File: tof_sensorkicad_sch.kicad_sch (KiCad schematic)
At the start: 1 part

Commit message: working on board
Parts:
- U2: footprint (none) -> 00_parts_lib:SATEL-VL53L8A
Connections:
- net +1.8VDC: now also U2.11 (IOVDD), U2.3 (CORE_1V8); no longer U2. (SDA)
- net +3.3VDC: now also U2.12 (AVDD); no longer U2. (SDA)
- net GND: now also U2.1 (DUT_GND), U2.7 (I2C_N); no longer U2. (SDA)
- net PWM_1: now also U2.4 (LPn); no longer U2. (SDA)
- net SCL: now also U2.8 (SCL); no longer U2. (SDA)
- net SDA: now also U2.6 (SDA); no longer U2. (SDA)
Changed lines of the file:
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@@
 		(dnp no)
 		(fields_autoplaced yes)
-		(property "Reference" "#PWR012"
+		(property "Reference" "#PWR014"
 			(at 165.1 113.03 0)
 			(effects
@@
 			(project ""
 				(path "/f7edb1cc-a42a-4cc0-9a6f-d9bd2b944353/74857e1b-d607-48d9-8b82-96dfc41384b6"
-					(reference "#PWR012")
+					(reference "#PWR014")
 					(unit 1)
 				)
@@
 			)
 		)
-		(property "Footprint" ""
+		(property "Footprint" "00_parts_lib:SATEL-VL53L8A"
 			(at 176.53 72.39 0)
 			(effects
@@
 			)
 		)
-		(pin ""
+		(pin "2"
 		)
-		(pin ""
+		(pin "3"
 		)
-		(pin ""
+		(pin "10"
 		)
-		(pin ""
+		(pin "8"
 		)
-		(pin ""
+		(pin "7"
 		)
-		(pin ""
+		(pin "11"
 		)
-		(pin ""
+		(pin "5"
 		)
-		(pin ""
+		(pin "1"
 		)
-		(pin ""
+		(pin "6"
 		)
-		(pin ""
+		(pin "9"
 		)
-		(pin ""
+		(pin "4"
 		)
-		(pin ""
+		(pin "12"
 		)
 		(instances

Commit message: made board
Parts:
- added TP10, TP11, TP12, TP13, TP14, TP9: TestPoint, TestPoint:TestPoint_Pad_D2.0mm, symbol Connector:TestPoint
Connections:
- net GND: now also TP12.1, TP13.1, TP14.1
- net PWM_1: now also TP11.1
- net SCL: now also TP9.1
- net SDA: now also TP10.1
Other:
- note added: "TEST POINTS"
- note added: "TOF CIRCUIT"
- moved on the sheet: U2

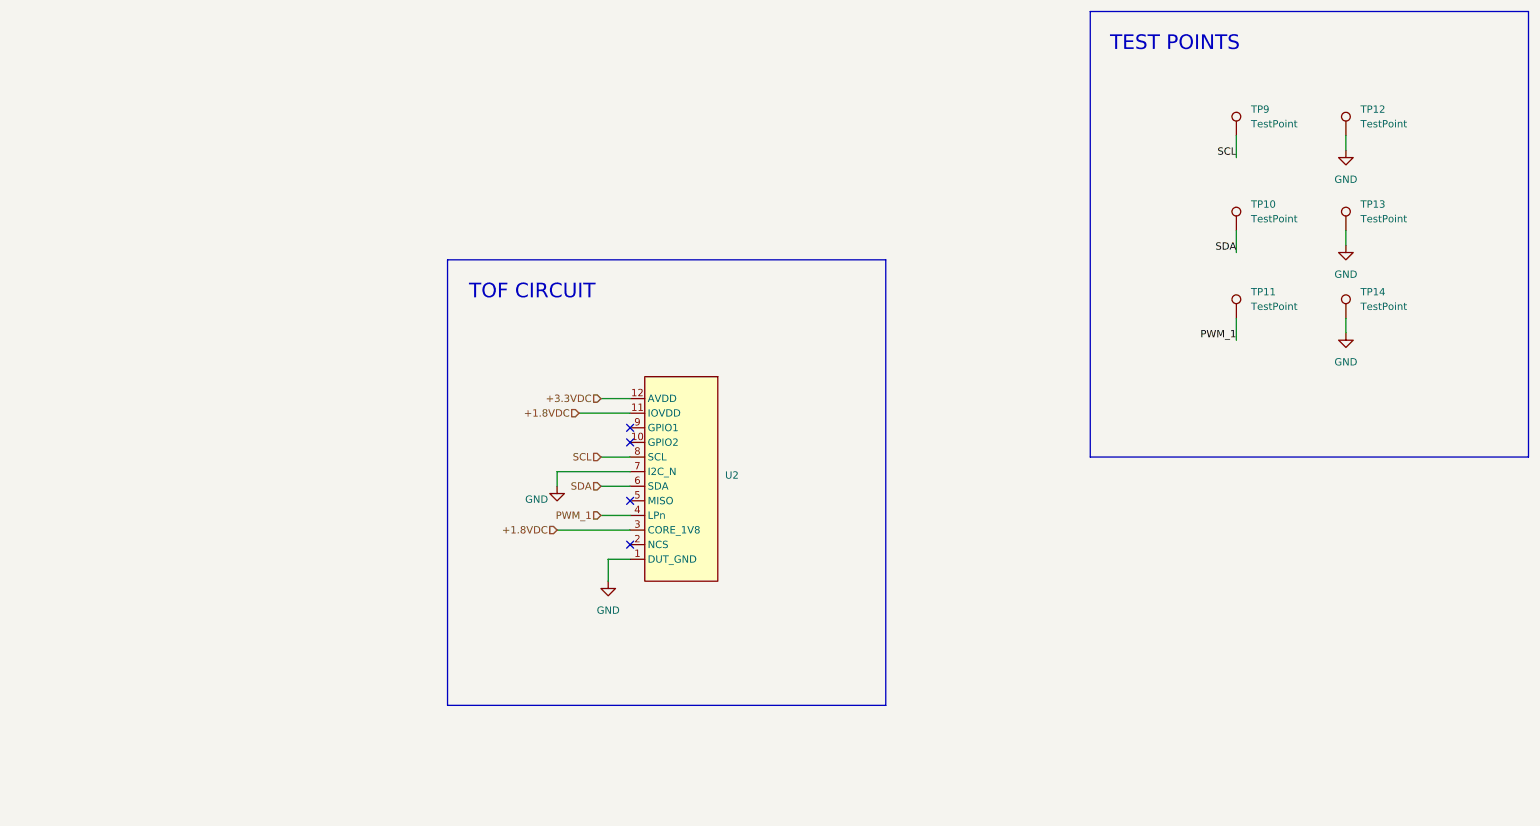
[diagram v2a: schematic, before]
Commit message: working on revisions
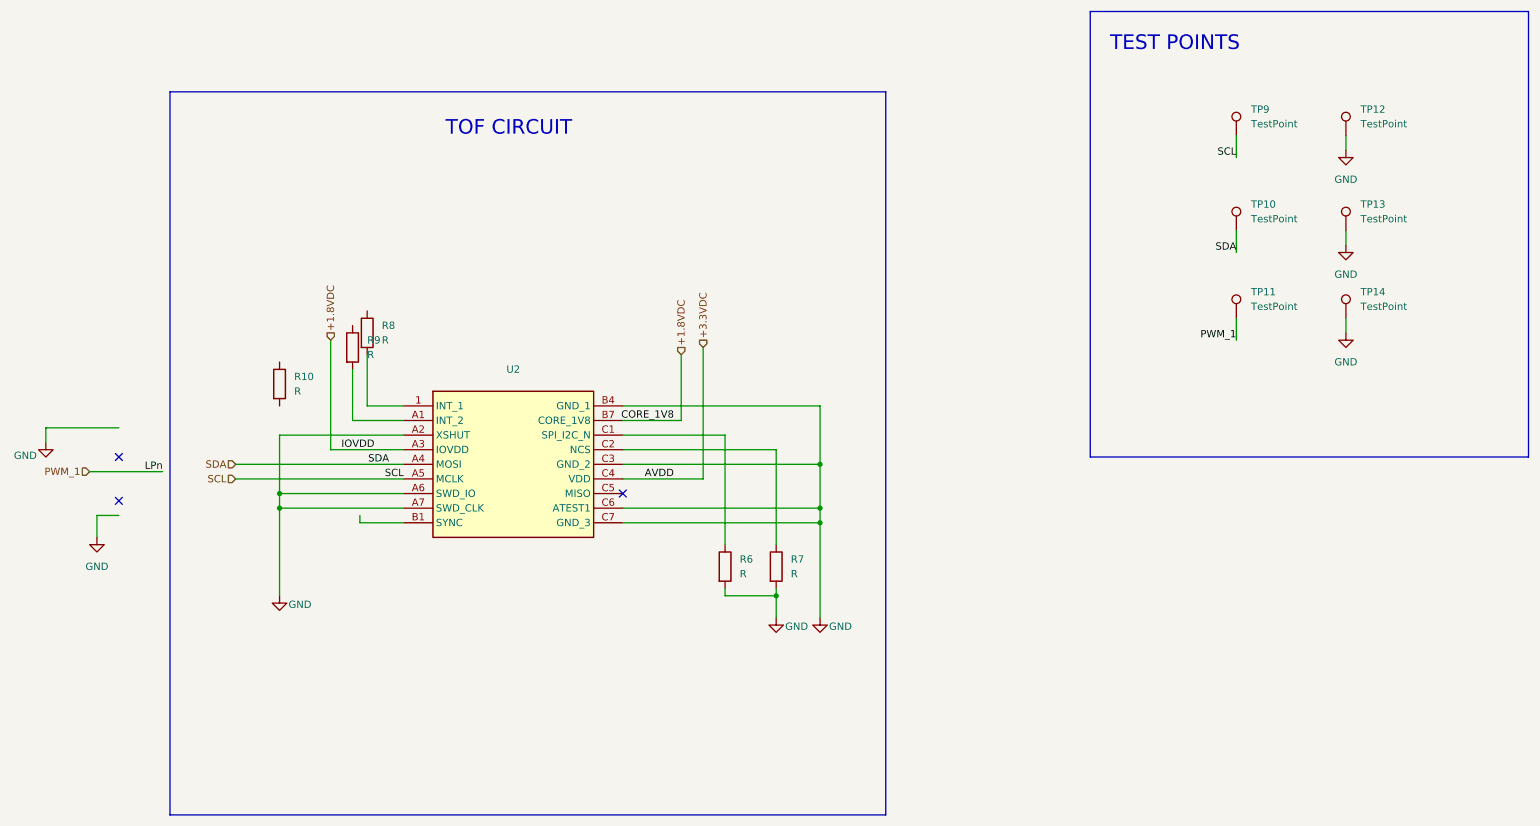
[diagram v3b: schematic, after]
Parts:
- added R10, R6, R7, R8, R9: R, Resistor_SMD:R_0805_2012Metric_Pad1.20x1.40mm_HandSolder, symbol Device:R
- U2: footprint 00_parts_lib:SATEL-VL53L8A -> VL53L8CXV0GC1; symbol 00_project_parts:SATEL-VL53L8A -> 00_project_parts:VL53L8CXV0GC_1; Height (none) -> 1.8; Manufacturer_Name (none) -> STMicroelectronics; Manufacturer_Part_Number (none) -> VL53L8CXV0GC/1; Mouser Part Number (none) -> 511-VL53L8CXV0GC/1; Mouser Price/Stock (none) -> https://www.mouser.co.uk/ProductDetail/STMicroelectronics/V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
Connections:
- net +1.8VDC: now also U2.A3 (IOVDD), U2.B7 (CORE_1V8); no longer U2.11 (IOVDD), U2.3 (CORE_1V8)
- net +3.3VDC: now also U2.C4 (VDD); no longer U2.12 (AVDD)
- net GND: now also U2.A2 (XSHUT), U2.A6 (SWD_IO), U2.A7 (SWD_CLK), U2.B4 (GND_1), U2.C3 (GND_2), U2.C6 (ATEST1), U2.C7 (GND_3), R6.2, R7.2; no longer U2.1 (DUT_GND), U2.7 (I2C_N)
- net PWM_1: no longer U2.4 (LPn)
- net SCL: now also U2.A5 (MCLK); no longer U2.8 (SCL)
- net SDA: now also U2.A4 (MOSI); no longer U2.6 (SDA)
- new net: R6.1, U2.C1 (SPI_I2C_N)
- new net: R8.2, U2.1 (INT_1)
- new net: R9.2, U2.A1 (INT_2)
- new net: R7.1, U2.C2 (NCS)
- no-connect marks 4 -> 3

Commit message: latest
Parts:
- removed R8: R, Resistor_SMD:R_0805_2012Metric_Pad1.20x1.40mm_HandSolder, symbol Device:R
- added C5, C6: 100nF, Capacitor_SMD:C_0805_2012Metric_Pad1.18x1.45mm_HandSolder, symbol Device:C
- added C7: 47uF, Capacitor_SMD:C_0805_2012Metric_Pad1.18x1.45mm_HandSolder, symbol Device:C
- added R10, R9: 47k, Resistor_SMD:R_0805_2012Metric_Pad1.20x1.40mm_HandSolder, symbol Device:R
- added R7: 2.2k, Resistor_SMD:R_0805_2012Metric_Pad1.20x1.40mm_HandSolder, symbol Device:R
- R11: renamed from R6; value R -> 47k
- R12: renamed from R7; value R -> 47k
- R6: renamed from R10; value R -> 2.2k
- R8: renamed from R9; value R -> 47k
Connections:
- net +1.8VDC: now also R6.1, R8.1, C5.2, C6.2, R10.1, R7.1, R9.1
- net +3.3VDC: now also C7.1
- net GND: now also C5.1, C6.1, C7.2; no longer U2.A2 (XSHUT)
- net PWM_1: now also R8.2, U2.A2 (XSHUT), U2.B1 (SYNC), R10.2
- net SCL: now also R6.2
- net SDA: now also R7.2
- net at U2.1 (INT_1): now also U2.A1 (INT_2), R9.2
- no-connect marks 3 -> 1
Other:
- moved on the sheet: R6, R8, TP10, TP11, TP12, TP13, TP14, TP9

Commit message: not working, reverting to old design
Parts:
- C7: value 47uF -> 4.7uF
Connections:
- net PWM_1: no longer R10.2, U2.B1 (SYNC)
- new net: R10.2, U2.B1 (SYNC)
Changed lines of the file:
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@@
+	)
+	(junction
+		(at 68.58 72.39)
+		(diameter 0)
+		(color 0 0 0 0)
 	)
 	(junction
@@
 	)
 	(junction
-		(at 58.42 72.39)
-		(diameter 0)
-		(color 0 0 0 0)
-	)
-	(junction
 		(at 63.5 72.39)
 		(diameter 0)
@@
 	)
 	(junction
-		(at 54.61 72.39)
-		(diameter 0)
-		(color 0 0 0 0)
-	)
-	(junction
 		(at 76.2 72.39)
 		(diameter 0)
@@
 	(wire
 		(pts
-			(xy 54.61 72.39) (xy 54.61 90.17)
+			(xy 54.61 66.04) (xy 54.61 90.17)
 		)
 		(stroke
@@
 	(wire
 		(pts
+			(xy 68.58 72.39) (xy 72.39 72.39)
+		)
+		(stroke
+			(width 0)
+			(type default)
+		)
+	)
+	(wire
+		(pts
 			(xy 48.26 87.63) (xy 72.39 87.63)
 		)
@@
 	(wire
 		(pts
-			(xy 54.61 66.04) (xy 54.61 72.39)
-		)
-		(stroke
-			(width 0)
-			(type default)
-		)
-	)
-	(wire
-		(pts
 			(xy 133.35 68.58) (xy 133.35 85.09)
 		)
@@
 	(wire
 		(pts
-			(xy 54.61 72.39) (xy 58.42 72.39)
-		)
-		(stroke
-			(width 0)
-			(type default)
-		)
-	)
-	(wire
-		(pts
 			(xy 125.73 68.58) (xy 121.92 68.58)
 		)
@@
 	(wire
 		(pts
-			(xy 63.5 72.39) (xy 72.39 72.39)
+			(xy 68.58 59.69) (xy 68.58 72.39)
+		)
+		(stroke
+			(width 0)
+			(type default)
+		)
+	)
+	(wire
+		(pts
+			(xy 63.5 72.39) (xy 68.58 72.39)
 		)
 		(stroke
@@
 	(label "PWM_1"
 		(at 208.28 116.84 180)
-		(fields_autoplaced yes)
 		(effects
 			(font
@@
 	(label "SDA"
 		(at 208.28 101.6 180)
-		(fields_autoplaced yes)
 		(effects
 			(font
@@
 	(label "CORE_1V8"
 		(at 132.08 85.09 180)
-		(fields_autoplaced yes)
 		(effects
 			(font
@@
 		)
 	)
-	(label "LPn"
-		(at 81.28 87.63 180)
-		(fields_autoplaced yes)
-		(effects
-			(font
-				(size 1.27 1.27)
-			)
-			(justify right bottom)
-		)
-	)
 	(label "IOVDD"
-		(at 77.47 90.17 180)
-		(fields_autoplaced yes)
+		(at 71.12 90.17 180)
 		(effects
 			(font
@@
 	(label "SDA"
 		(at 85.09 92.71 180)
-		(fields_autoplaced yes)
 		(effects
 			(font
@@
 	(label "SCL"
 		(at 85.09 95.25 180)
-		(fields_autoplaced yes)
 		(effects
 			(font
@@
 	(label "SCL"
 		(at 208.28 85.09 180)
-		(fields_autoplaced yes)
 		(effects
 			(font
@@
 	(label "AVDD"
 		(at 127 95.25 0)
-		(fields_autoplaced yes)
 		(effects
 			(font
@@
 		(shape input)
 		(at 52.07 95.25 180)
-		(fields_autoplaced yes)
 		(effects
 			(font
@@
 		(shape input)
 		(at 52.07 92.71 180)
-		(fields_autoplaced yes)
 		(effects
 			(font
@@
 			)
 			(justify right)
+		)
+	)
+	(hierarchical_label "+1.8VDC"
+		(shape input)
+		(at 68.58 59.69 90)
+		(effects
+			(font
+				(size 1.27 1.27)
+			)
+			(justify left)
 		)
 	)
@@
 		(shape input)
 		(at 138.43 58.42 90)
-		(fields_autoplaced yes)
 		(effects
 			(font
@@
 		(shape input)
 		(at 133.35 58.42 90)
-		(fields_autoplaced yes)
 		(effects
 			(font
@@
 		(shape input)
 		(at 54.61 59.69 90)
-		(fields_autoplaced yes)
 		(effects
 			(font
@@
 		(shape input)
 		(at 48.26 87.63 180)
-		(fields_autoplaced yes)
 		(effects
 			(font
@@
 			)
 		)
-		(property "Value" "47uF"
+		(property "Value" "4.7uF"
 			(at 145.034 65.024 90)
 			(effects

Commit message: latest updates, up to v2
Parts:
- removed C5, C6: 100nF, Capacitor_SMD:C_0805_2012Metric_Pad1.18x1.45mm_HandSolder, symbol Device:C
- removed C7: 4.7uF, Capacitor_SMD:C_0805_2012Metric_Pad1.18x1.45mm_HandSolder, symbol Device:C
- removed R10, R11, R12, R8, R9: 47k, Resistor_SMD:R_0805_2012Metric_Pad1.20x1.40mm_HandSolder, symbol Device:R
- removed R6, R7: 2.2k, Resistor_SMD:R_0805_2012Metric_Pad1.20x1.40mm_HandSolder, symbol Device:R
- removed TP10, TP11, TP12, TP13, TP14, TP9: TestPoint, TestPoint:TestPoint_Pad_D2.0mm, symbol Connector:TestPoint
- U2: footprint VL53L8CXV0GC1 -> 00_parts_lib:SATEL-VL53L8A; symbol 00_project_parts:VL53L8CXV0GC_1 -> 00_project_parts:SATEL-VL53L8A; Height 1.8 -> (none); Manufacturer_Name STMicroelectronics -> (none); Manufacturer_Part_Number VL53L8CXV0GC/1 -> (none); Mouser Part Number 511-VL53L8CXV0GC/1 -> (none); Mouser Price/Stock https://www.mouser.co.uk/ProductDetail/STMicroelectronics/V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 -> (none)
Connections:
- net +1.8VDC: now also U2.11 (IOVDD), U2.3 (CORE_1V8); no longer U2.A3 (IOVDD), U2.B7 (CORE_1V8)
- net +3.3VDC: now also U2.12 (AVDD); no longer U2.C4 (VDD)
- net GND: now also U2.1 (DUT_GND), U2.7 (I2C_N); no longer U2.A6 (SWD_IO), U2.A7 (SWD_CLK), U2.B4 (GND_1), U2.C3 (GND_2), U2.C6 (ATEST1), U2.C7 (GND_3)
- net PWM_1: now also U2.4 (LPn); no longer U2.A2 (XSHUT)
- net SCL: now also U2.8 (SCL); no longer U2.A5 (MCLK)
- net SDA: now also U2.6 (SDA); no longer U2.A4 (MOSI)
- no-connect marks 1 -> 4
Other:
- note removed: "TEST POINTS"
